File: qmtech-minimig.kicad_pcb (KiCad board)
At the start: 4 copper layers, 142.2 x 92 mm, 141 parts, among them IC1 RTL8211EG-VB-CG, J1 DB9_Male, J2 DB9_Male, J3 SCHA5B0200, J4 ARM_JTAG, J5 AUDIO-CONNECTOR-6P-SMD-344003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, J6 Mini-DIN-6, J8 HR911130A, J9 47151-0001, SW1 SW_Push, U1 MCU-STM32F407VET6(LQFP100), U2 QM_XC7A35T_DDR3, U3 LT1963AxST-1.8, Y1 Crystal, Y2 Crystal

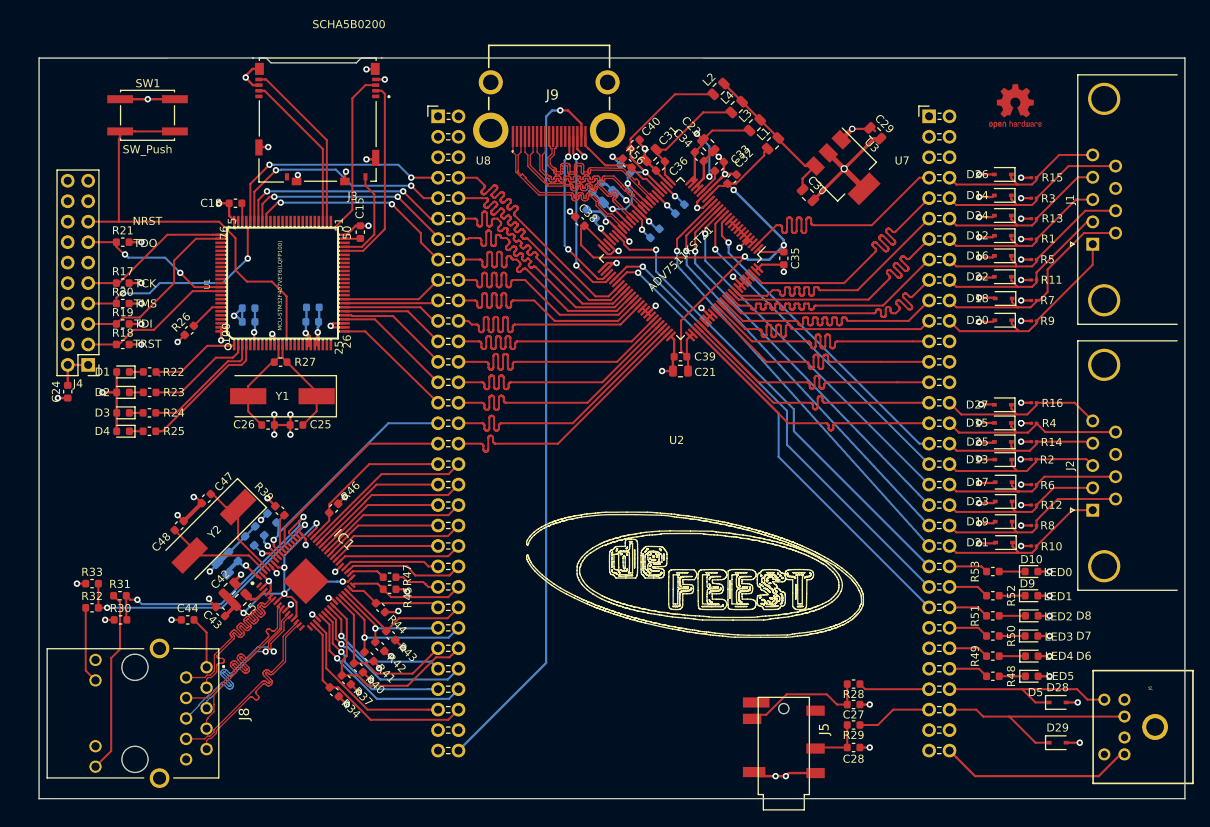
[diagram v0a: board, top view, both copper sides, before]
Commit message: First step to implement floppy interface. ESP32 check wireing in.
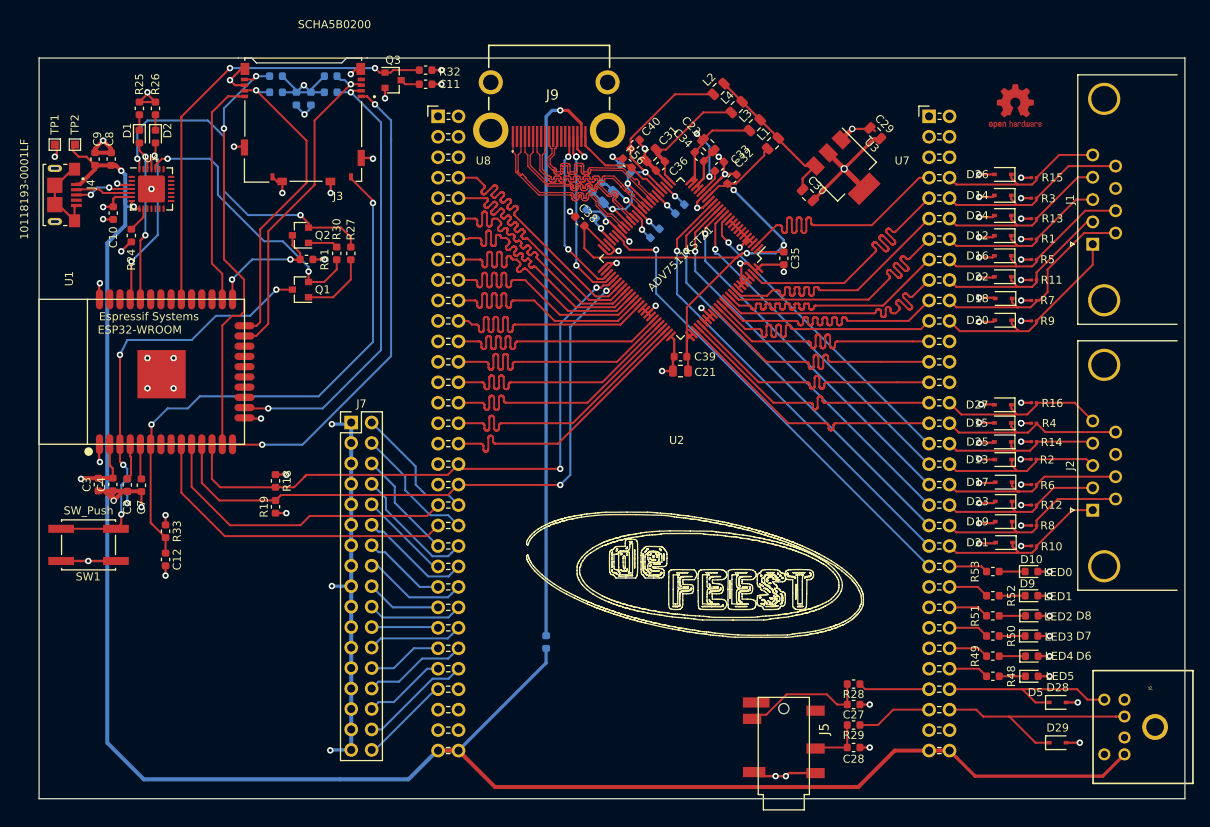
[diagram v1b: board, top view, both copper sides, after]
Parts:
- removed C14, C16, C24, C43, C44, C46: 100nF, Capacitor_SMD:C_0603_1608Metric
- removed C15, C18: 2.2uF, Capacitor_SMD:C_0603_1608Metric
- removed C19: 1uF, Capacitor_SMD:C_0603_1608Metric
- removed C20: 4.7uF, Capacitor_SMD:C_0603_1608Metric
- removed C25, C26, C47, C48: 22pF, Capacitor_SMD:C_0603_1608Metric
- removed C42, C45: 4.7uF, Capacitor_SMD:C_0805_2012Metric
- removed D3, D4: LED, LED_SMD:LED_0603_1608Metric
- removed IC1: RTL8211EG-VB-CG, RTL8211EG:QFN50P900X900X100-65N-D
- removed J8: HR911130A, HR911130A:HR911130A
- removed L5: L, Inductor_SMD:L_0805_2012Metric
- removed R35: 2.49K, Resistor_SMD:R_0603_1608Metric
- removed R36, R37, R38, R39, R40, R41, R42, R43, R44, R45, R46: 4.7K, Resistor_SMD:R_0603_1608Metric
- removed R47: 100, Resistor_SMD:R_0603_1608Metric
- removed Y1, Y2: Crystal, Crystal:Crystal_SMD_HC49-SD
- added C10: 100nF, Capacitor_SMD:C_0603_1608Metric, F.Cu at (60.0, 82.5)
- added C11: C, Capacitor_SMD:C_0603_1608Metric, F.Cu at (98.8, 66.5)
- added C12: 100n, Capacitor_SMD:C_0603_1608Metric, F.Cu at (66.5, 125.5)
- added C2: 100nF, Capacitor_SMD:C_0603_1608Metric, F.Cu at (61.8, 116.2)
- added C3: 100nF, Capacitor_SMD:C_0603_1608Metric, F.Cu at (58.1, 116.2)
- added C4: 1uF, Capacitor_SMD:C_0603_1608Metric, F.Cu at (60.0, 116.2)
- added C5: 100nF, Capacitor_SMD:C_0603_1608Metric, B.Cu at (84.5, 68.3)
- added C6: 100nF, Capacitor_SMD:C_0603_1608Metric, B.Cu at (82.8, 68.3)
- added C7: 100nF, Capacitor_SMD:C_0603_1608Metric, F.Cu at (63.5, 116.3)
- added C8: 100nF, Capacitor_SMD:C_0603_1608Metric, F.Cu at (59.8, 75.8)
- added C9: 4.7uF, Capacitor_SMD:C_0603_1608Metric, F.Cu at (57.8, 75.8)
- added J7: Conn_02x13_Odd_Even, Connector_PinHeader_2.54mm:PinHeader_2x17_P2.54mm_Vertical, F.Cu at (89.5, 108.5)
- added Q1: MMBT2222A, Package_TO_SOT_SMD:SOT-23, F.Cu at (83.2, 92.0)
- added Q2: MMBT2222A, Package_TO_SOT_SMD:SOT-23, F.Cu at (83.2, 85.2)
- added Q3: BSS84, Package_TO_SOT_SMD:SOT-23, F.Cu at (94.8, 66.0)
- added TP1: TestPoint, TestPoint:TestPoint_Pad_1.0x1.0mm, F.Cu at (52.8, 74.0)
- added TP2: TestPoint, TestPoint:TestPoint_Pad_1.0x1.0mm, F.Cu at (55.2, 74.0)
- added U4: INTERFACE-CP2102-GMR(QFN28), Package_DFN_QFN:QFN-28-1EP_5x5mm_P0.5mm_EP3.35x3.35mm, F.Cu at (64.8, 79.5)
- D1, D2: value LED -> GREEN
- J4: value ARM_JTAG -> 10118193-0001LF; footprint Connector_PinHeader_2.54mm:PinHeader_2x10_P2.54mm_Vertical -> 10118193-001:FCI_10118193-0001LF
- R17: moved to B.Cu
- R18, R19: value 10K -> 4.7k
- R20, R21: value 10K -> 10k; moved to B.Cu
- R22, R23: value 1k -> 10k; moved to B.Cu
- R24: value 1k -> 10k
- R26: value 10k -> 1k
- R27: value 1M -> 10k
- R30: value 4.7K -> 10k
- R31: value 530 -> 10k
- R32: value 530 -> 100k
- R33: value 4.7K -> 10K
- R34: value 4.7K -> 10k; moved to B.Cu
- U1: value MCU-STM32F407VET6(LQFP100) -> ESP32-WROOM; footprint stm32f407:LQFP100-0.5-13.8X13.8MM -> ESP32:ESP32-WROOM
- moved R32 78.6 mm to (98.8, 64.8), turned to 180 degrees
- moved SW1 53.8 mm to (56.9, 123.7), turned to 180 degrees
- moved R30 52.8 mm to (87.8, 87.5), turned to 270 degrees
- moved R31 47.7 mm to (84.0, 88.2)
- moved R22 41.4 mm to (87.0, 67.5), turned to 0 degrees
- moved R23 40.4 mm to (80.2, 67.5)
- moved R25 40.1 mm to (63.2, 69.5), turned to 270 degrees
- moved R20 34.0 mm to (80.2, 65.5), turned to 180 degrees
- moved R21 33.0 mm to (87.0, 65.5)
- moved D2 32.0 mm to (65.2, 73.0), turned to 270 degrees
- moved R19 29.6 mm to (80.2, 119.0), turned to 90 degrees
- moved D1 29.3 mm to (63.2, 73.0), turned to 270 degrees
- moved R26 27.9 mm to (65.2, 69.5), turned to 270 degrees
- moved R34 27.0 mm to (113.8, 135.8), turned to 90 degrees
- moved R18 25.4 mm to (80.2, 115.8), turned to 270 degrees
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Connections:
- net ADV_CEC renamed Net-(J9-Pad13)
- D1 pad 2: 3V3 -> ESP_UART0_RX
- D2 pad 2: 3V3 -> ESP_UART0_TX
- J3 pad 1: Net-(J3-Pad1) -> ESP_SD_DATA2
- J3 pad 2: SD_SPI2_CS -> ESP_SD_DATA3
- J3 pad 3: SD_SPI2_MOSI -> ESP_SD_CMD
- J3 pad 4: 3V3 -> Net-(C11-Pad2)
- J3 pad 5: SD_SPI2_SCK -> ESP_SD_CLK
- J3 pad 7: SD_SPI2_MISO -> ESP_SD_DATA0
- J3 pad 8: Net-(J3-Pad8) -> ESP_SD_DATA1
- J3 pad CMN: Net-(J3-PadCMN) -> GND
- J3 pad DT: SD_SW -> ESP_SD_SW
- J4 pad 1: 3V3 -> VIN5V
- J4 pad 2: 3V3 -> Net-(J4-Pad2)
- J4 pad 3: /MCU/JTAG_TRST -> Net-(J4-Pad3)
- J4 pad 4: GND -> Net-(J4-Pad4)
- J4 pad 5: /MCU/JTAG_TDI -> GND
- J9 pad 18: VIN5V -> Net-(J9-Pad18)
- R17 pad 1: /MCU/JTAG_TCK -> 3V3
- R17 pad 2: GND -> ESP_RST
- R18 pad 1: /MCU/JTAG_TRST -> 3V3
- R18 pad 2: 3V3 -> ADV_SCL
- R19 pad 1: /MCU/JTAG_TDI -> 3V3
- R19 pad 2: 3V3 -> ADV_SDA
- R20 pad 1: /MCU/JTAG_TMS -> 3V3
- R20 pad 2: 3V3 -> ESP_SD_CLK
- R21 pad 1: /MCU/JTAG_TDO -> 3V3
- R21 pad 2: 3V3 -> ESP_SD_CMD
- R22 pad 1: /MCU/LED0 -> 3V3
- R22 pad 2: Net-(D1-Pad1) -> ESP_SD_DATA3
- R23 pad 1: /MCU/LED1 -> 3V3
- R23 pad 2: Net-(D2-Pad1) -> ESP_SD_DATA0
- R24 pad 1: /MCU/LED2 -> Net-(R24-Pad1)
- R24 pad 2: Net-(D3-Pad1) -> 3V3
- R25 pad 1: /MCU/LED3 -> GND
- R25 pad 2: Net-(D4-Pad1) -> Net-(D1-Pad1)
- R26 pad 2: Net-(R26-Pad2) -> Net-(D2-Pad1)
- R27 pad 1: Net-(C26-Pad2) -> Net-(Q1-Pad1)
- R27 pad 2: Net-(C25-Pad2) -> USB_DTR
- R30 pad 1: GND -> Net-(Q2-Pad1)
- R30 pad 2: ETH_LED1 -> USB_RTS
- R31 pad 1: Net-(J8-Pad11) -> ESP_FLASH
- R31 pad 2: ETH_LED1 -> 3V3
- R32 pad 1: Net-(J8-Pad13) -> 3V3
- R32 pad 2: ETH_LED0 -> ESP_SD_VCC_EN
- R33 pad 2: ETH_LED0 -> ESP_SD_SW
- R34 pad 1: ETH_RXDV -> VIN5V
- R34 pad 2: GND -> Net-(J9-Pad18)
- SW1 pad 2: /MCU/NRST -> ESP_RST
- U1 pad 1: /MCU/LED0 -> GND
- U1 pad 10: GND -> ESP_UART1_RX
- U1 pad 11: GND -> ADV_SDA
- U1 pad 12: Net-(C26-Pad2) -> ADV_SCL
- U1 pad 13: Net-(C25-Pad2) -> ESP_SD_CLK
- U1 pad 14: /MCU/NRST -> ESP_SD_DATA2
- U1 pad 15: Net-(U1-Pad15) -> GND
- U1 pad 16: Net-(U1-Pad16) -> ESP_SD_DATA3
- U1 pad 19: GND -> Net-(U1-Pad19)
- U1 pad 2: /MCU/LED1 -> 3V3
- U1 pad 20: GND -> Net-(U1-Pad20)
- U1 pad 21: 3V3 -> Net-(U1-Pad21)
- U1 pad 22: 3V3 -> Net-(U1-Pad22)
- U1 pad 23: Net-(U1-Pad23) -> ESP_SD_CMD
- U1 pad 24: Net-(U1-Pad24) -> ESP_SD_DATA0
- U1 pad 25: Net-(U1-Pad25) -> ESP_FLASH
- U1 pad 26: STM_SPI1_CS -> ESP_SD_DATA1
- U1 pad 27: GND -> Net-(U1-Pad27)
- U1 pad 28: GND -> Net-(U1-Pad28)
- U1 pad 29: STM_SPI1_NSS -> Net-(U1-Pad29)
- U1 pad 3: /MCU/LED2 -> ESP_RST
- U1 pad 30: STM_SPI1_SCK -> ESP_SD_VCC_EN
- U1 pad 31: STM_SPI1_MISO -> Net-(U1-Pad31)
- U1 pad 32: STM_SPI1_MOSI -> Net-(U1-Pad32)
- U1 pad 33: STM_IO_33 -> Net-(U1-Pad33)
- U1 pad 34: STM_IO_34 -> ESP_UART0_RX
- U1 pad 35: Net-(U1-Pad35) -> ESP_UART0_TX
- U1 pad 38: Net-(U1-Pad38) -> GND
- U1 pad 39: Net-(U1-Pad39) -> GND
- U1 pad 4: /MCU/LED3 -> Net-(C2-Pad1)
- U1 pad 6: 3V3 -> ESP_SD_SW
- U1 pad 9: Net-(U1-Pad9) -> ESP_UART1_TX
- U2 pad U731: ETH_INTB -> Net-(U2-PadU731)
- U2 pad U733: ETH_MDIO -> Net-(U2-PadU733)
- U2 pad U735: ETH_TXER -> Net-(U2-PadU735)
- U2 pad U736: ETH_TXD7 -> ADV_SCL
- U2 pad U737: ETH_TXD6 -> Net-(U2-PadU737)
- U2 pad U738: ETH_TXD5 -> ADV_SDA
- U2 pad U739: ETH_TXD4 -> ESP_UART1_RX
- U2 pad U740: ETH_TXDCLK -> EXP_02
- U2 pad U741: ETH_TXD3 -> ESP_UART1_TX
- U2 pad U742: ETH_TXD2 -> EXP_04
- U2 pad U743: ETH_TXD1 -> EXP_06
- U2 pad U744: ETH_PHYRSTB -> EXP_08
- U2 pad U745: ETH_TXD0 -> EXP_10
- U2 pad U746: ETH_TXEN -> EXP_12
- U2 pad U747: ETH_GTX_CLK -> EXP_14
- U2 pad U748: ETH_CRS -> EXP_16
- U2 pad U749: ETH_COL_MODE -> EXP_18
- U2 pad U750: ETH_RXER -> EXP_20
- U2 pad U751: ETH_RXD7 -> EXP_22
- U2 pad U752: ETH_RXD6 -> EXP_24
- U2 pad U753: ETH_RXD5 -> EXP_26
- U2 pad U754: ETH_RXD4 -> EXP_28
- U2 pad U755: ETH_RXC -> EXP_30
- U2 pad U756: ETH_RXD3 -> EXP_32
- U2 pad U757: ETH_RXD2 -> EXP_34
- U2 pad U758: ETH_RXD1 -> Net-(U2-PadU758)
- U2 pad U759: ETH_RXD0 -> Net-(U2-PadU759)
- U2 pad U760: ETH_RXDV -> Net-(U2-PadU760)
- U2 pad U847: ADV_SCL -> Net-(U2-PadU847)
- U2 pad U849: ADV_SDA -> Net-(U2-PadU849)
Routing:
- net VIN5V: track 114.3 -> 243.1 mm, vias 1 -> 2
- net Net-(J9-Pad18): track 0.00 -> 71.5 mm, vias 0 -> 1
- net ESP_SD_SW: track 0.00 -> 70.3 mm, vias 0 -> 2
- net GND: track 231.7 -> 293.3 mm, vias 76 -> 71
- net ESP_SD_DATA2: track 0.00 -> 58.7 mm, vias 0 -> 2
- net ESP_SD_DATA3: track 0.00 -> 56.9 mm, vias 0 -> 2
- net /MCU/NRST: track 56.6 -> 0.00 mm
- net ESP_SD_VCC_EN: track 0.00 -> 55.1 mm, vias 0 -> 2
- net ESP_RST: track 0.00 -> 54.5 mm, vias 0 -> 4
- net ESP_SD_CLK: track 0.00 -> 53.7 mm, vias 0 -> 2
- net USB_DTR: track 0.00 -> 43.4 mm, vias 0 -> 2
- net ESP_SD_CMD: track 0.00 -> 41.0 mm, vias 0 -> 1
- net ESP_UART1_TX: track 0.00 -> 40.7 mm
- net ETH_REG_OUT_OUT: track 40.0 -> 0.00 mm, vias 5 -> 0
- net ESP_SD_DATA0: track 0.00 -> 39.9 mm, vias 0 -> 1
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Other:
- board size 142.2 x 92 mm -> 142.2 x 91.9 mm
- board text removed: "NRST"
- board text removed: "TCK"
- board text removed: "TDI"
- board text removed: "TDO"
- board text removed: "TMS"
- board text removed: "TRST"

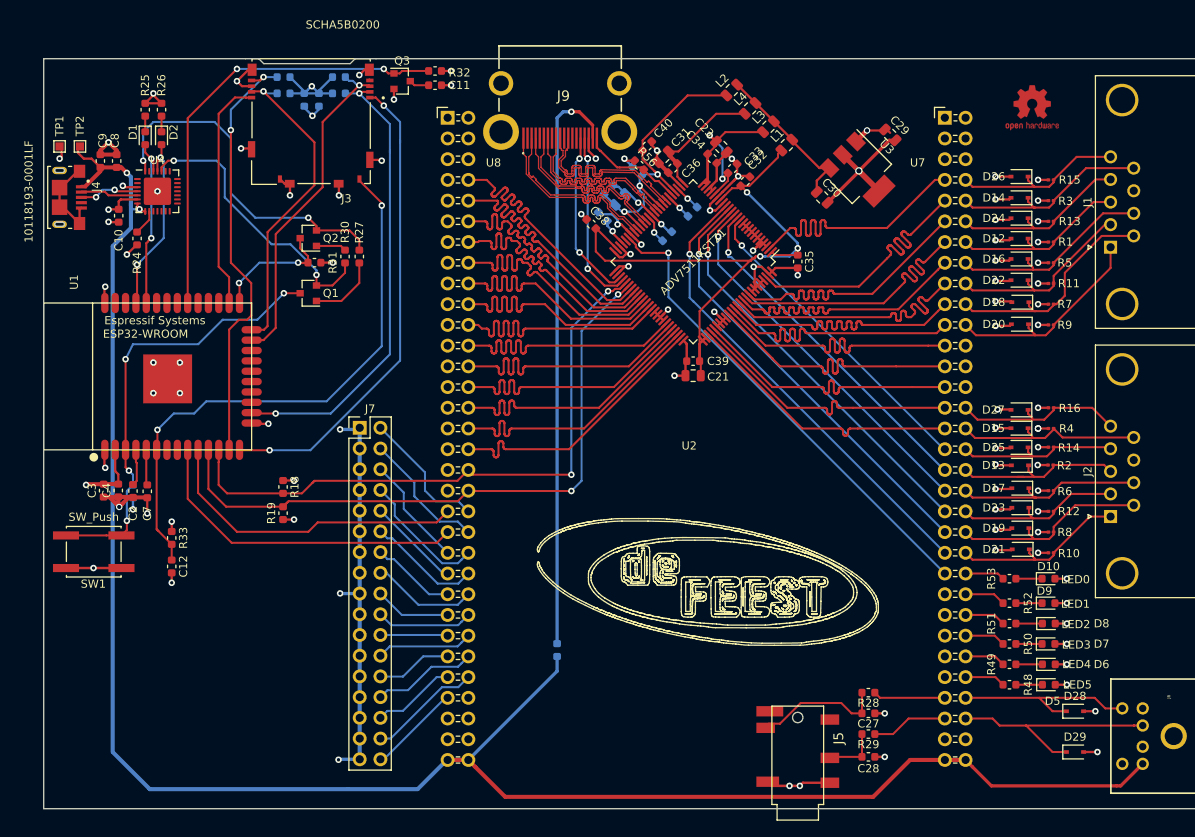
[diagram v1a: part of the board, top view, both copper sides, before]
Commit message: Integrated the Rover V2 into the board, added level shifters for the floppy interface.
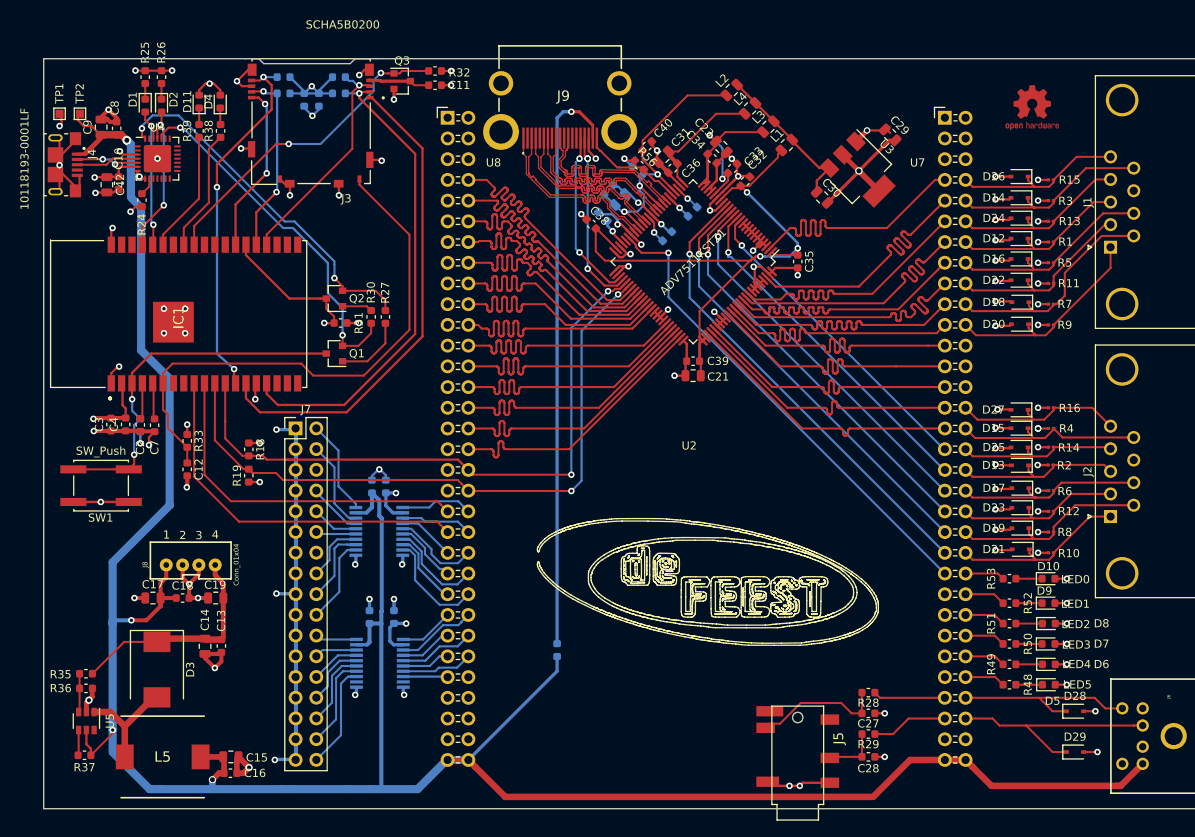
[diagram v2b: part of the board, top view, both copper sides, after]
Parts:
- removed U1: ESP32-WROOM, ESP32:ESP32-WROOM
- added C13: 100nF, Capacitor_SMD:C_0603_1608Metric, F.Cu at (72.6, 135.2)
- added C14: 22uF, Capacitor_SMD:C_0805_2012Metric, F.Cu at (70.6, 135.3)
- added C15: 22uF, Capacitor_SMD:C_0805_2012Metric, F.Cu at (73.8, 148.8)
- added C16: 100nF, Capacitor_SMD:C_0603_1608Metric, F.Cu at (73.7, 150.8)
- added C17: 22uF, Capacitor_SMD:C_0805_2012Metric, F.Cu at (64.2, 129.4)
- added C18: 100nF, Capacitor_SMD:C_0603_1608Metric, F.Cu at (67.8, 129.4)
- added C19: 22uF, Capacitor_SMD:C_0805_2012Metric, F.Cu at (71.9, 129.4)
- added C20: 100nF, Capacitor_SMD:C_0603_1608Metric, B.Cu at (92.8, 115.7)
- added C24: 100nF, Capacitor_SMD:C_0603_1608Metric, B.Cu at (91.0, 115.7)
- added C25: 100nF, Capacitor_SMD:C_0603_1608Metric, B.Cu at (93.8, 131.7)
- added C26: 100nF, Capacitor_SMD:C_0603_1608Metric, B.Cu at (90.8, 131.7)
- added C42: 4.7uF, Capacitor_SMD:C_0805_2012Metric, F.Cu at (58.5, 78.7)
- added D11: LED4, LED_SMD:LED_0603_1608Metric, F.Cu at (69.9, 68.5)
- added D3: SS34_Zener, Diode_SMD:D_SMC, F.Cu at (64.7, 138.2)
- added D4: LED5, LED_SMD:LED_0603_1608Metric, F.Cu at (72.5, 68.5)
- added IC1: ESP32-WROVER-B_(16MB), ESP32-WROVER-B_(16MB):ESP32WROVERIB16MB, F.Cu at (67.3, 95.2)
- added J8: Conn_01x04, Connectors:JST-4-PTH-VERT, F.Cu at (68.8, 124.8)
- added L5: 22uH, CDRH104RNP-220NC:INDPM102100X400N, F.Cu at (65.4, 148.8)
- added R35: 63k, Resistor_SMD:R_0603_1608Metric, F.Cu at (56.0, 138.7)
- added R36: 3.3k, Resistor_SMD:R_0603_1608Metric, F.Cu at (56.0, 140.4)
- added R37: 10k, Resistor_SMD:R_0603_1608Metric, F.Cu at (55.8, 148.7)
- added R38: 1k, Resistor_SMD:R_0603_1608Metric, F.Cu at (72.5, 72.1)
- added R39: 1k, Resistor_SMD:R_0603_1608Metric, F.Cu at (69.8, 72.1)
- added U5: MT3608, Package_TO_SOT_SMD:SOT-23-6, F.Cu at (56.0, 144.4)
- added U6: TXS0108EPWR, TXS0108EPWR:SOP65P640X120-20N, B.Cu at (92.0, 121.2)
- added U7: TXS0108EPWR, TXS0108EPWR:SOP65P640X120-20N, B.Cu at (92.0, 137.4)
- C9: footprint Capacitor_SMD:C_0603_1608Metric -> Capacitor_SMD:C_0805_2012Metric
- moved C12 12.1 mm to (68.4, 113.6)
- moved R33 12.1 mm to (68.4, 110.1)
- moved C3 8.15 mm to (59.0, 108.1)
- moved C7 8.15 mm to (64.4, 108.2)
- moved C2 8.15 mm to (62.6, 108.2)
- moved C4 8.15 mm to (60.9, 108.1)
- moved R17 8.15 mm to (62.6, 108.2)
- moved SW1 8.15 mm to (57.8, 115.6)
- moved Q1 8.06 mm to (86.5, 99.4)
- moved R27 8.06 mm to (92.7, 94.9)
- moved R30 8.06 mm to (91.0, 94.9)
- moved R31 8.06 mm to (87.2, 95.7)
- moved Q2 8.06 mm to (86.4, 92.7)
- moved J7 7.86 mm to (81.7, 108.6)
- moved R19 6.23 mm to (75.9, 114.4)
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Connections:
- net Net-(J4-Pad2) renamed /MCU/D-
- net Net-(J4-Pad3) renamed /MCU/D+
- C10 pad 1: 3V3 -> GND
- C10 pad 2: GND -> 3V3
- J7 pad 10: EXP_10 -> H_EXP_10
- J7 pad 12: EXP_12 -> H_EXP_12
- J7 pad 14: EXP_14 -> H_EXP_14
- J7 pad 16: EXP_16 -> H_EXP_16
- J7 pad 18: EXP_18 -> H_EXP_18
- J7 pad 2: EXP_02 -> H_EXP_02
- J7 pad 20: EXP_20 -> H_EXP_20
- J7 pad 22: EXP_22 -> H_EXP_22
- J7 pad 24: EXP_24 -> H_EXP_24
- J7 pad 26: EXP_26 -> H_EXP_26
- J7 pad 28: EXP_28 -> H_EXP_28
- J7 pad 30: EXP_30 -> H_EXP_30
- J7 pad 32: EXP_32 -> H_EXP_32
- J7 pad 34: EXP_34 -> H_EXP_34
- J7 pad 4: EXP_04 -> H_EXP_04
- J7 pad 6: EXP_06 -> H_EXP_06
- J7 pad 8: EXP_08 -> H_EXP_08
- U2 pad U743: EXP_06 -> EXP_08
- U2 pad U744: EXP_08 -> EXP_10
- U2 pad U745: EXP_10 -> EXP_12
- U2 pad U746: EXP_12 -> EXP_16
- U2 pad U747: EXP_14 -> EXP_18
- U2 pad U748: EXP_16 -> EXP_20
- U2 pad U749: EXP_18 -> EXP_22
- U2 pad U750: EXP_20 -> EXP_24
- U2 pad U751: EXP_22 -> EXP_26
- U2 pad U752: EXP_24 -> EXP_28
- U2 pad U753: EXP_26 -> EXP_30
- U2 pad U754: EXP_28 -> EXP_32
- U2 pad U755: EXP_30 -> EXP_34
- U2 pad U756: EXP_32 -> Net-(U2-PadU756)
- U2 pad U757: EXP_34 -> Net-(U2-PadU757)
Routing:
- net VIN5V: track 243.1 -> 327.2 mm, vias 2 -> 5
- net GND: track 293.3 -> 331.3 mm, vias 71 -> 84
- net VIN12V: track 0.00 -> 27.4 mm
- net 3V3: track 105.2 -> 124.2 mm, vias 36 -> 41
- net ESP_SD_DATA0: track 39.9 -> 22.9 mm, vias 1 -> 2
- net ESP_SD_VCC_EN: track 55.1 -> 39.7 mm
- net /MCU/LED1: track 0.00 -> 15.0 mm
- net /MCU/LED0: track 0.00 -> 15.0 mm
- net EXP_06: track 13.7 -> 0.00 mm
- net Net-(D3-Pad2): track 0.00 -> 13.6 mm
- net ESP_SD_CMD: track 41.0 -> 27.7 mm
- net H_EXP_34: track 0.00 -> 13.3 mm
- net H_EXP_02: track 0.00 -> 11.7 mm
- net H_EXP_32: track 0.00 -> 11.3 mm
- net H_EXP_04: track 0.00 -> 11.0 mm
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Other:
- net class Power high added: clearance 0.15, trace_width 0.5, via_dia 0.9, via_drill 0.5
- board text added: "1"
- board text added: "2"
- board text added: "3"
- board text added: "4"
